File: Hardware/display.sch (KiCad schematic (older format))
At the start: 2 parts, among them P1 CONN_8

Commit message: added support for MI0283QT-2 display and improved main layout
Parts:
- removed LCD1: S65, welectronic-S65, symbol S65
- removed P1: CONN_8, symbol CONN_8
- added P1: CONN_10X2, symbol CONN_10X2
- added P2: CONN_2X2, symbol CONN_2X2
- added U1: MI0283QT-2, symbol MI0283QT-2
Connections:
- net labels added: CS, IM0, IM1, IM2, IM3, LED1, LED2, LED3, LED4, MISO, MOSI, RD, RESET, RS, SCK, VCC, X+, X-, Y+, Y-
- net labels removed: +1.8V, +12V
- wire segments 24 -> 48

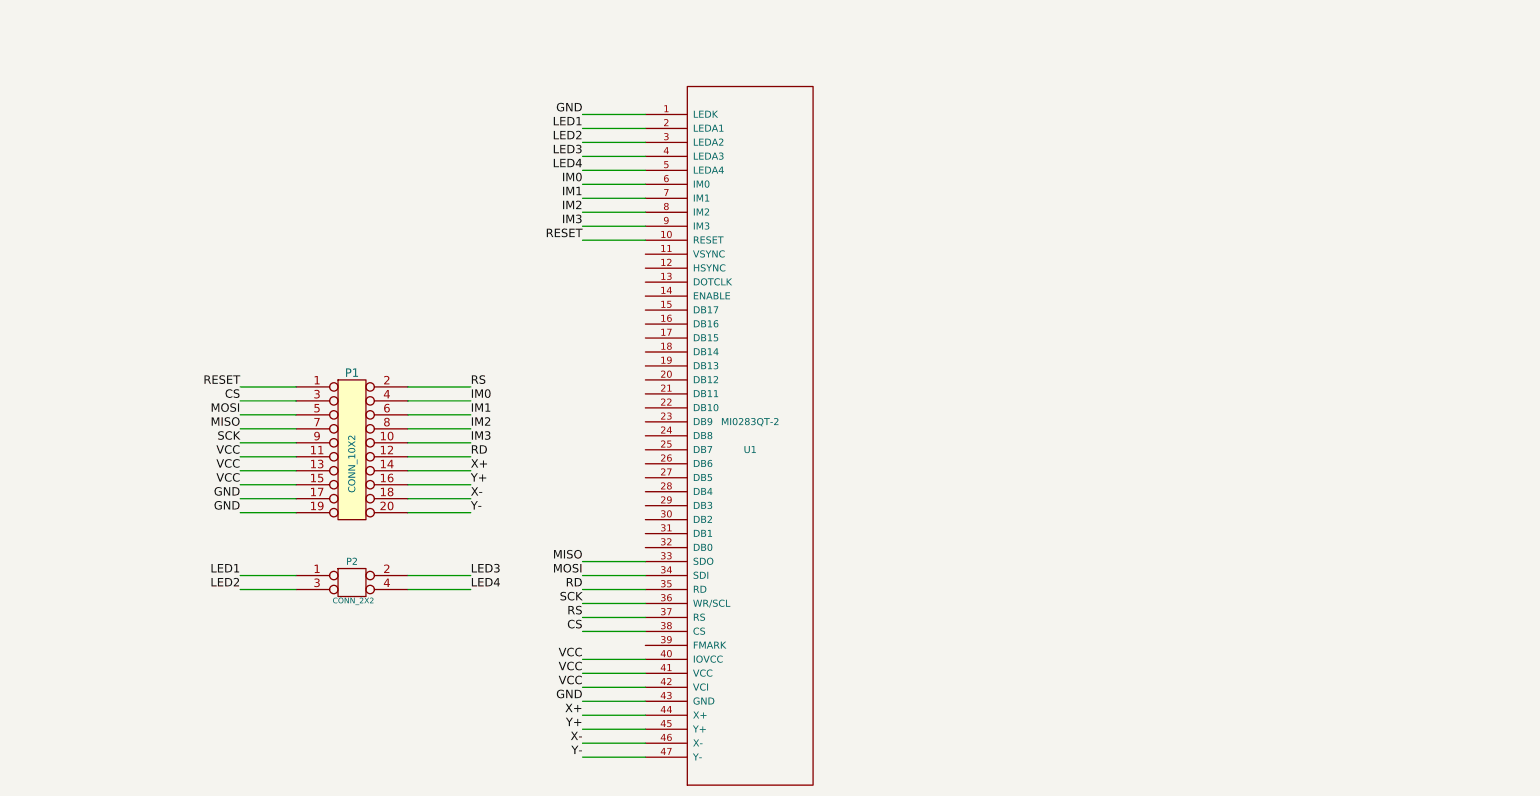
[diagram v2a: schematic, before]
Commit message: Angepasster Displayadapter und erste Testversion der Software. Display, SDCard,Reed funktionieren.
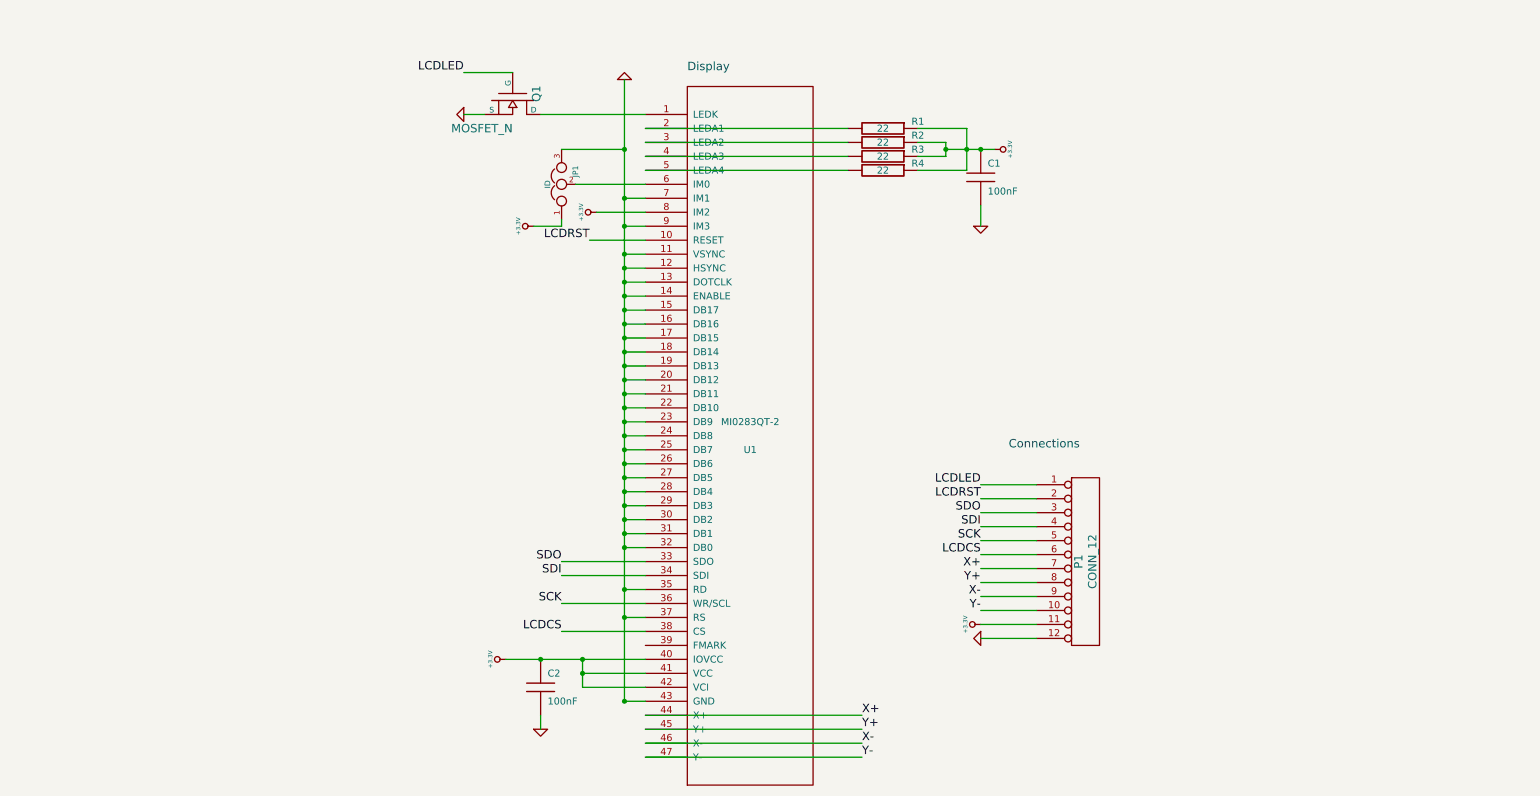
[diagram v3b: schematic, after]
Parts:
- removed P1: CONN_10X2, symbol CONN_10X2
- removed P2: CONN_2X2, symbol CONN_2X2
- added C1, C2: 100nF, symbol C
- added JP1: ID, symbol JUMPER3
- added P1: CONN_12, symbol CONN_12
- added Q1: MOSFET_N, symbol MOSFET_N
- added R1, R2, R3, R4: 22, symbol R
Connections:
- net IM1 is gone; now on net GND: U1.7 (IM1)
- net IM3 is gone; now on net GND: U1.9 (IM3)
- net RD is gone; now on net GND: U1.35 (RD)
- net RS is gone; now on net GND: U1.37 (RS)
- net VCC is gone; now on net +3.3V: U1.40 (IOVCC), U1.41 (VCC), U1.42 (VCI)
- net GND: now also U1.11 (VSYNC), U1.12 (HSYNC), U1.13 (DOTCLK), U1.14 (ENABLE), U1.15 (DB17), U1.16 (DB16), U1.17 (DB15), U1.18 (DB14), U1.19 (DB13), U1.20 (DB12), U1.21 (DB11), U1.22 (DB10), U1.23 (DB9), U1.24 (DB8), U1.25 (DB7), U1.26 (DB6), U1.27 (DB5), U1.28 (DB4), U1.29 (DB3), U1.30 (DB2), U1.31 (DB1), U1.32 (DB0), C1.2, C2.2, JP1.3, P1.12 (P12), Q1.S; no longer U1.1 (LEDK)
- net SCK: now also P1.5 (P5)
- net X+: now also P1.7 (P7)
- net X-: now also P1.9 (P9)
- net Y+: now also P1.8 (P8)
- net Y-: now also P1.10 (P10)
- net CS renamed LCDCS
- net LCDCS: now also P1.6 (P6)
- net IM0: no longer names the net of U1.6 (IM0)
- net IM0: now also JP1.2
- net IM2 renamed +3.3V
- net +3.3V: now also C1.1, C2.1, JP1.1, P1.11 (P11), R1.1, R2.1, R3.1, R4.1
- net LED1: no longer names the net of U1.2 (LEDA1)
- net LED1: now also R1.2
- net LED2: no longer names the net of U1.3 (LEDA2)
- net LED2: now also R2.2
- net LED3: no longer names the net of U1.4 (LEDA3)
- net LED3: now also R3.2
- net LED4: no longer names the net of U1.5 (LEDA4)
- net LED4: now also R4.2
- net MISO renamed SDO
- net SDO: now also P1.3 (P3)
- net MOSI renamed SDI
- net SDI: now also P1.4 (P4)
- net RESET renamed LCDRST
- net LCDRST: now also P1.2 (P2)
- new net: Q1.D, U1.1 (LEDK)
- new net LCDLED: P1.1 (P1), Q1.G
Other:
- note added: "Connections"
- note added: "Display"

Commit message: added capacitors to all vcc pins
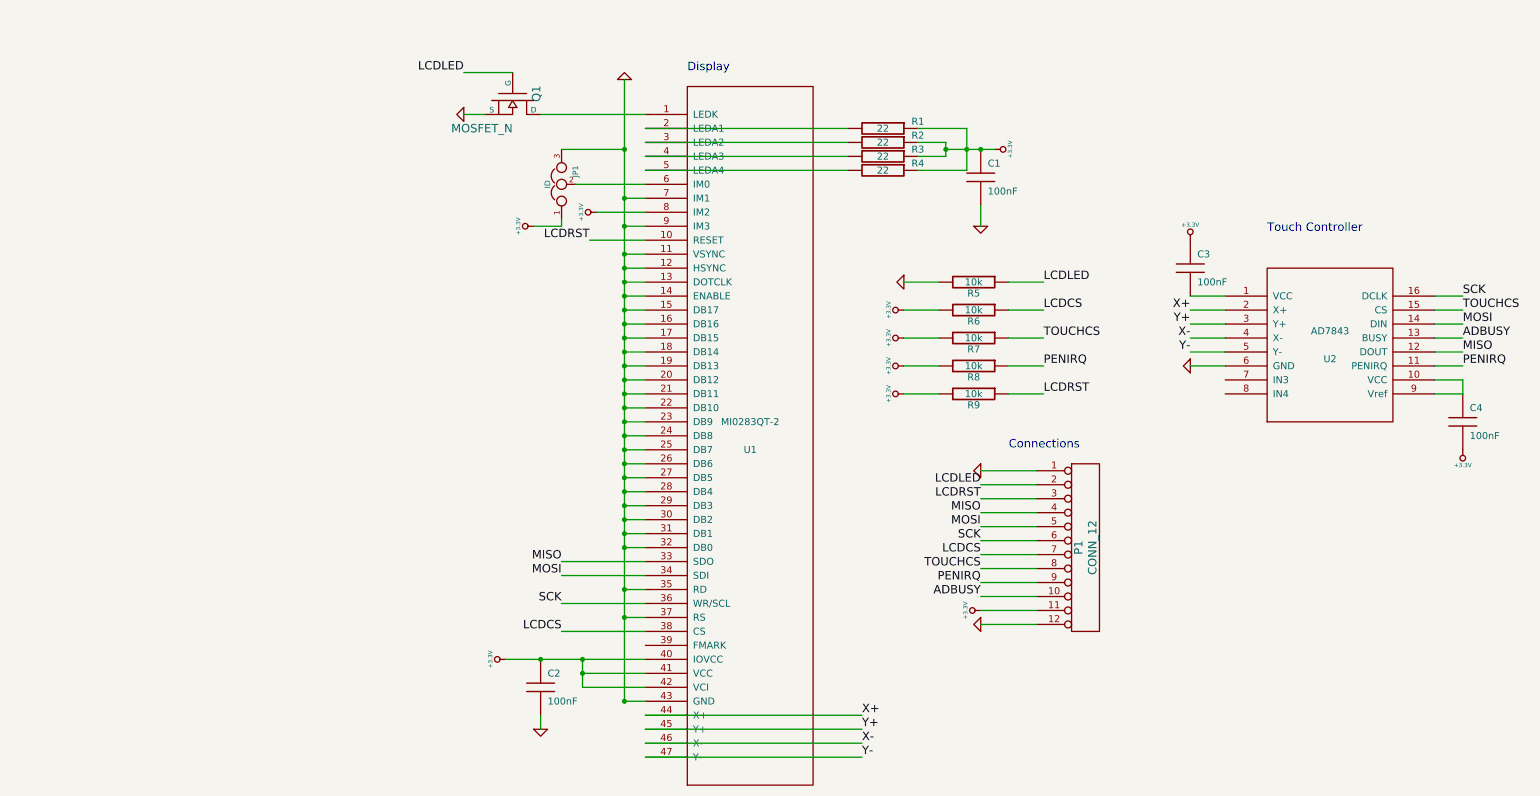
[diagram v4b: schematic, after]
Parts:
- added C3, C4: 100nF, symbol C
- added R5, R6, R7, R8, R9: 10k, symbol R
- added U2: AD7843, symbol AD7843
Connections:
- net +3.3V: now also C3.1, C4.2, R6.2, R7.2, R8.2, R9.2
- net GND: now also P1.1 (P1), R5.2, U2.6 (GND)
- net LCDCS: now also P1.7 (P7), R6.1; no longer P1.6 (P6)
- net LCDLED: now also P1.2 (P2), R5.1; no longer P1.1 (P1)
- net LCDRST: now also P1.3 (P3), R9.1; no longer P1.2 (P2)
- net SCK: now also P1.6 (P6), U2.16 (DCLK); no longer P1.5 (P5)
- net X+: now also U2.2 (X+); no longer P1.7 (P7)
- net X-: now also U2.4 (X-); no longer P1.9 (P9)
- net Y+: now also U2.3 (Y+); no longer P1.8 (P8)
- net Y-: now also U2.5 (Y-); no longer P1.10 (P10)
- net SDI renamed MISO
- net MISO: now also U1.33 (SDO), U2.12 (DOUT); no longer U1.34 (SDI)
- removed net SDO: P1.3 (P3), U1.33 (SDO)
- new net: C3.2, U2.1 (VCC)
- new net: C4.1, U2.10 (VCC), U2.9 (Vref)
- new net ADBUSY: P1.10 (P10), U2.13 (BUSY)
- new net MOSI: P1.5 (P5), U1.34 (SDI), U2.14 (DIN)
- new net PENIRQ: P1.9 (P9), R8.1, U2.11 (PENIRQ)
- new net TOUCHCS: P1.8 (P8), R7.1, U2.15 (CS)
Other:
- note added: "Touch Controller"
